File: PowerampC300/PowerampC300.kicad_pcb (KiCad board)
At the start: 2 copper layers, 240 x 63 mm, 103 parts, among them J1 Conn_01x02, J2 Conn_01x02, J3 Conn_01x02, J4 Conn_01x01, J5 Conn_01x01, J6 Conn_01x01, J7 Conn_01x01, J8 Conn_01x02, J9 Conn_Coaxial, Q1 BC546, Q10 MJE15033, Q11 MJE15032, Q12 MJE15032, Q13 BC546, Q14 BC556, Q15 MJE15032, Q16 MJE15033, Q17 MJL3281A, Q18 MJL1302A, Q19 MJL3281A, Q2 BC546, Q20 MJL1302A, Q21 MJL3281A, Q22 MJL1302A, Q23 MJL3281A, Q24 MJL1302A, Q3 BC556, Q4 BC556, Q5 BC546, Q6 BC546, Q7 BC546, Q8 MPSA92, Q9 BC556

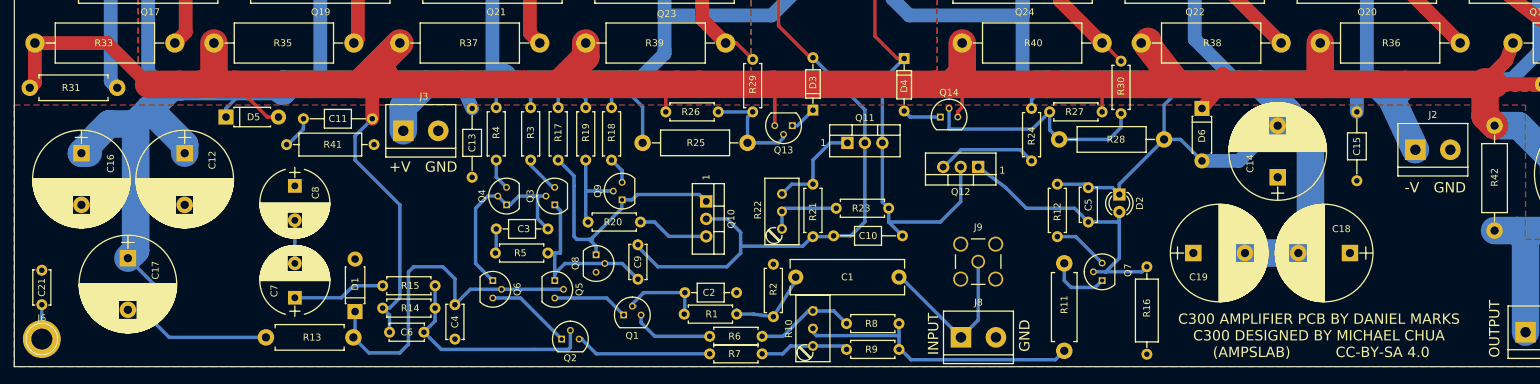
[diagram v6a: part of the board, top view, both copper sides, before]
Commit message: Changed to 2N5551/2N5401 from BC546C/BC556C transistors
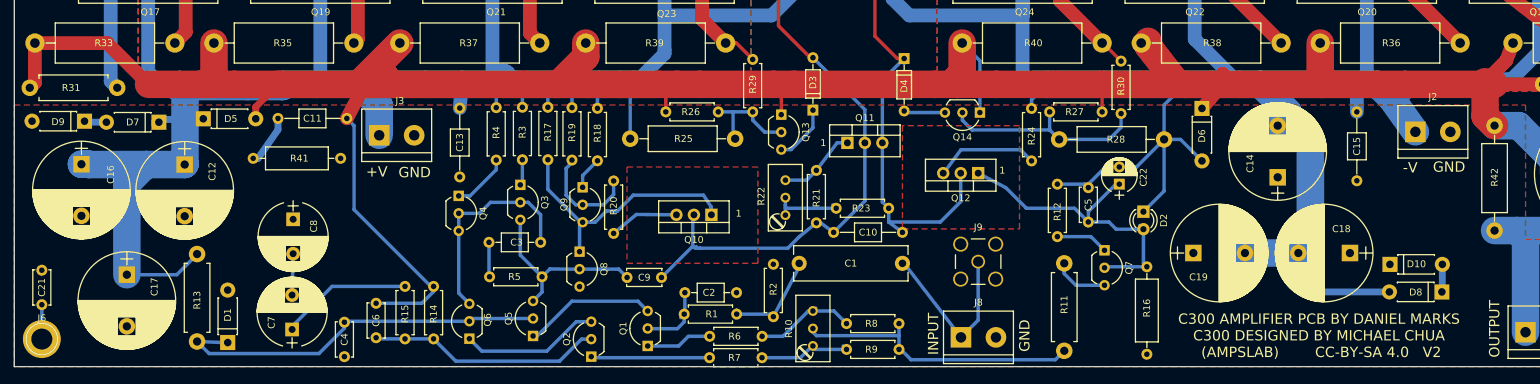
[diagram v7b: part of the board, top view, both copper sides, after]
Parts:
- added C22: 47 uF, Capacitors_THT:CP_Radial_D5.0mm_P2.50mm, F.Cu at (186.5, 79.5)
- added D10: 1N4755A, Diodes_THT:D_DO-41_SOD81_P7.62mm_Horizontal, F.Cu at (225.8, 91.2)
- added D7: 1N4755A, Diodes_THT:D_DO-41_SOD81_P7.62mm_Horizontal, F.Cu at (47.0, 70.5)
- added D8: 1N4755A, Diodes_THT:D_DO-41_SOD81_P7.62mm_Horizontal, F.Cu at (233.3, 95.2)
- added D9: 1N4755A, Diodes_THT:D_DO-41_SOD81_P7.62mm_Horizontal, F.Cu at (36.2, 70.3)
- Q1, Q13, Q2, Q5, Q6, Q7: value BC546 -> 2N5551; footprint TO_SOT_Packages_THT:TO-92_Molded_Narrow -> TO_SOT_Packages_THT:TO-92_Inline_Wide
- Q14, Q3, Q4, Q9: value BC556 -> 2N5401; footprint TO_SOT_Packages_THT:TO-92_Molded_Narrow -> TO_SOT_Packages_THT:TO-92_Inline_Wide
- Q8: value MPSA92 -> 2N5401; footprint TO_SOT_Packages_THT:TO-92_Molded_Narrow -> TO_SOT_Packages_THT:TO-92_Inline_Wide
- R42: value 3k3 -> 4R7
- moved R13 22.7 mm to (52.5, 102.3), turned to 90 degrees
- moved D1 19.0 mm to (57.0, 102.5)
- moved C4 16.3 mm to (74.0, 104.5)
- moved Q6 9.11 mm to (92.1, 102.0), turned to 90 degrees
- moved Q5 8.64 mm to (101.3, 101.5), turned to 90 degrees
- moved R14 8.04 mm to (86.9, 94.3), turned to 270 degrees
- moved Q4 7.07 mm to (90.5, 81.2), turned to 270 degrees
- moved C6 7.00 mm to (78.5, 101.8), turned to 90 degrees
- moved Q9 6.01 mm to (108.5, 80.0), turned to 270 degrees
- moved Q14 5.79 mm to (166.2, 69.1), turned to 180 degrees
- moved Q3 5.78 mm to (99.5, 79.6), turned to 270 degrees
- moved Q1 5.70 mm to (118.0, 103.0), turned to 90 degrees
- moved R41 5.25 mm to (73.4, 75.8)
- moved Q2 5.00 mm to (109.8, 104.5), turned to 90 degrees
- moved C8 4.86 mm to (66.5, 84.6)
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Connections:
- Q13 pad 1: Net-(D3-Pad1) -> Net-(C11-Pad2)
- Q13 pad 3: Net-(C11-Pad2) -> Net-(D3-Pad1)
- Q14 pad 1: Net-(D4-Pad2) -> Net-(C11-Pad2)
- Q14 pad 3: Net-(C11-Pad2) -> Net-(D4-Pad2)
- Q3 pad 1: Net-(C9-Pad1) -> Net-(Q3-Pad1)
- Q3 pad 3: Net-(Q3-Pad3) -> Net-(C9-Pad1)
- Q4 pad 1: Net-(C3-Pad2) -> Net-(Q4-Pad1)
- Q4 pad 3: Net-(Q4-Pad3) -> Net-(C3-Pad2)
- Q5 pad 1: Net-(C9-Pad1) -> Net-(Q1-Pad3)
- Q5 pad 3: Net-(Q1-Pad1) -> Net-(C9-Pad1)
- Q6 pad 1: Net-(C3-Pad2) -> Net-(Q2-Pad3)
- Q6 pad 3: Net-(Q2-Pad1) -> Net-(C3-Pad2)
- Q9 pad 1: Net-(Q10-Pad1) -> Net-(Q9-Pad1)
- Q9 pad 3: Net-(Q9-Pad3) -> Net-(Q10-Pad1)
- R11 pad 1: Net-(Q7-Pad1) -> Net-(Q7-Pad3)
- R12 pad 2: Net-(Q7-Pad3) -> Net-(Q7-Pad1)
- R18 pad 1: Net-(Q9-Pad3) -> Net-(Q9-Pad1)
- R3 pad 1: Net-(Q3-Pad3) -> Net-(Q3-Pad1)
- R4 pad 1: Net-(Q4-Pad3) -> Net-(Q4-Pad1)
- R6 pad 2: Net-(Q1-Pad3) -> Net-(Q1-Pad1)
- R7 pad 2: Net-(Q2-Pad3) -> Net-(Q2-Pad1)
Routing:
- net +48V: track 316.2 -> 291.1 mm
- net -48V: track 298.9 -> 308.8 mm
- net Net-(C10-Pad2): track 89.5 -> 80.9 mm
- net Net-(Q4-Pad1): track 0.00 -> 8.42 mm
- net Net-(Q1-Pad3): track 12.1 -> 19.5 mm
- net Net-(Q9-Pad1): track 0.00 -> 5.95 mm
- net Net-(C7-Pad1): track 13.5 -> 19.3 mm
- net Net-(Q2-Pad1): track 12.5 -> 18.2 mm
- net Net-(Q3-Pad3): track 5.58 -> 0.00 mm
- net Net-(C4-Pad2): track 52.0 -> 57.0 mm
- net Net-(C22-Pad1): track 43.1 -> 47.9 mm
- net Net-(Q4-Pad3): track 4.58 -> 0.00 mm
- net Net-(D3-Pad1): track 3.93 -> 8.47 mm
- net Net-(Q14-Pad2): track 35.0 -> 30.7 mm
- net Net-(Q9-Pad3): track 4.22 -> 0.00 mm
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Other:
- board text added: "C300 AMPLIFIER PCB BY DANIEL MARKS C300 DESIGNED BY MICHAEL CHUA (AMPSLAB) CC-BY-SA 4.0 V2"
- board text removed: "C300 AMPLIFIER PCB BY DANIEL MARKS C300 DESIGNED BY MICHAEL CHUA (AMPSLAB) CC-BY-SA 4.0"
